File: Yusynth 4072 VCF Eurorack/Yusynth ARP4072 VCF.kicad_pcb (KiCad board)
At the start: 2 copper layers, 85 parts, among them J1 Audio In 1, J2 Audio In 2, J3 V/Oct, J4 CV 1, J5 CV 2, J6 Audio In 1, J7 CONN_02X05, Q1 MMDT3906, Q2 MMDT3906, Q3 MMDT3906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

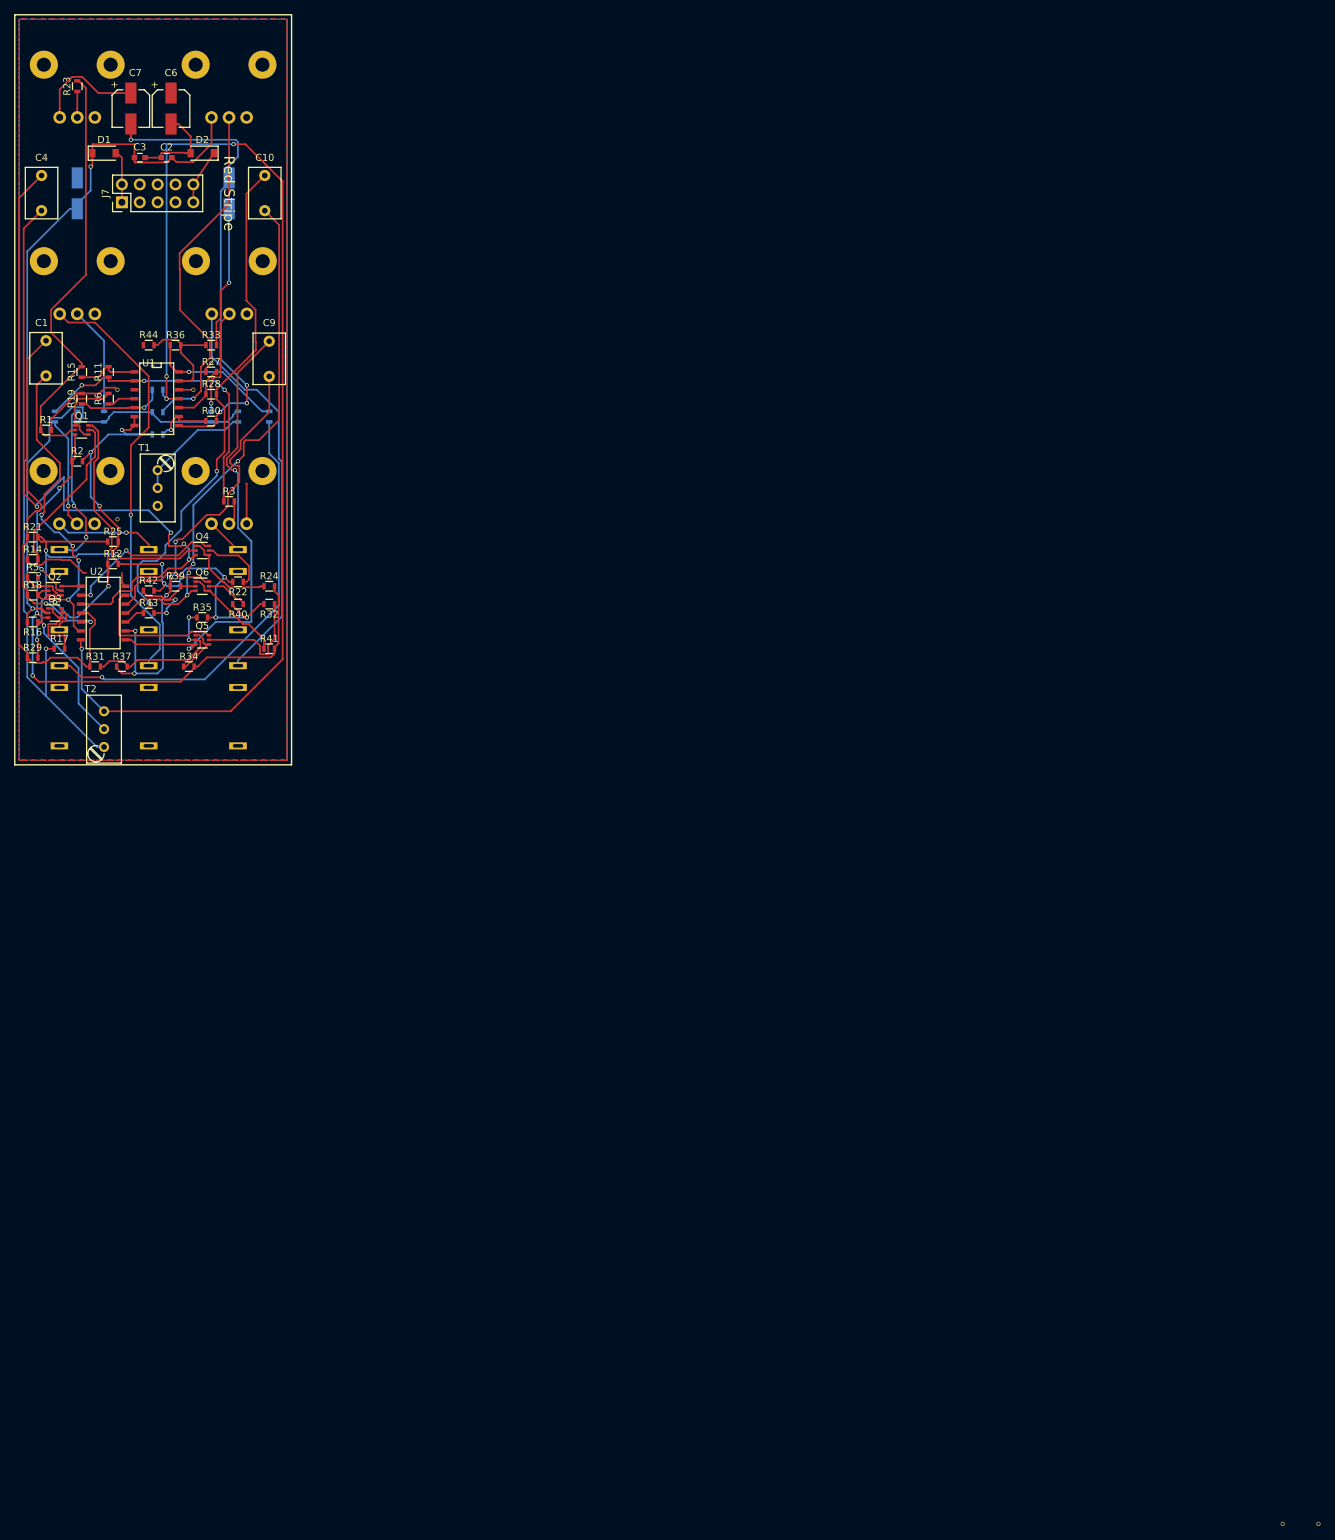
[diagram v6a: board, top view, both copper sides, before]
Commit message: Fixed some surprise DRC complaints
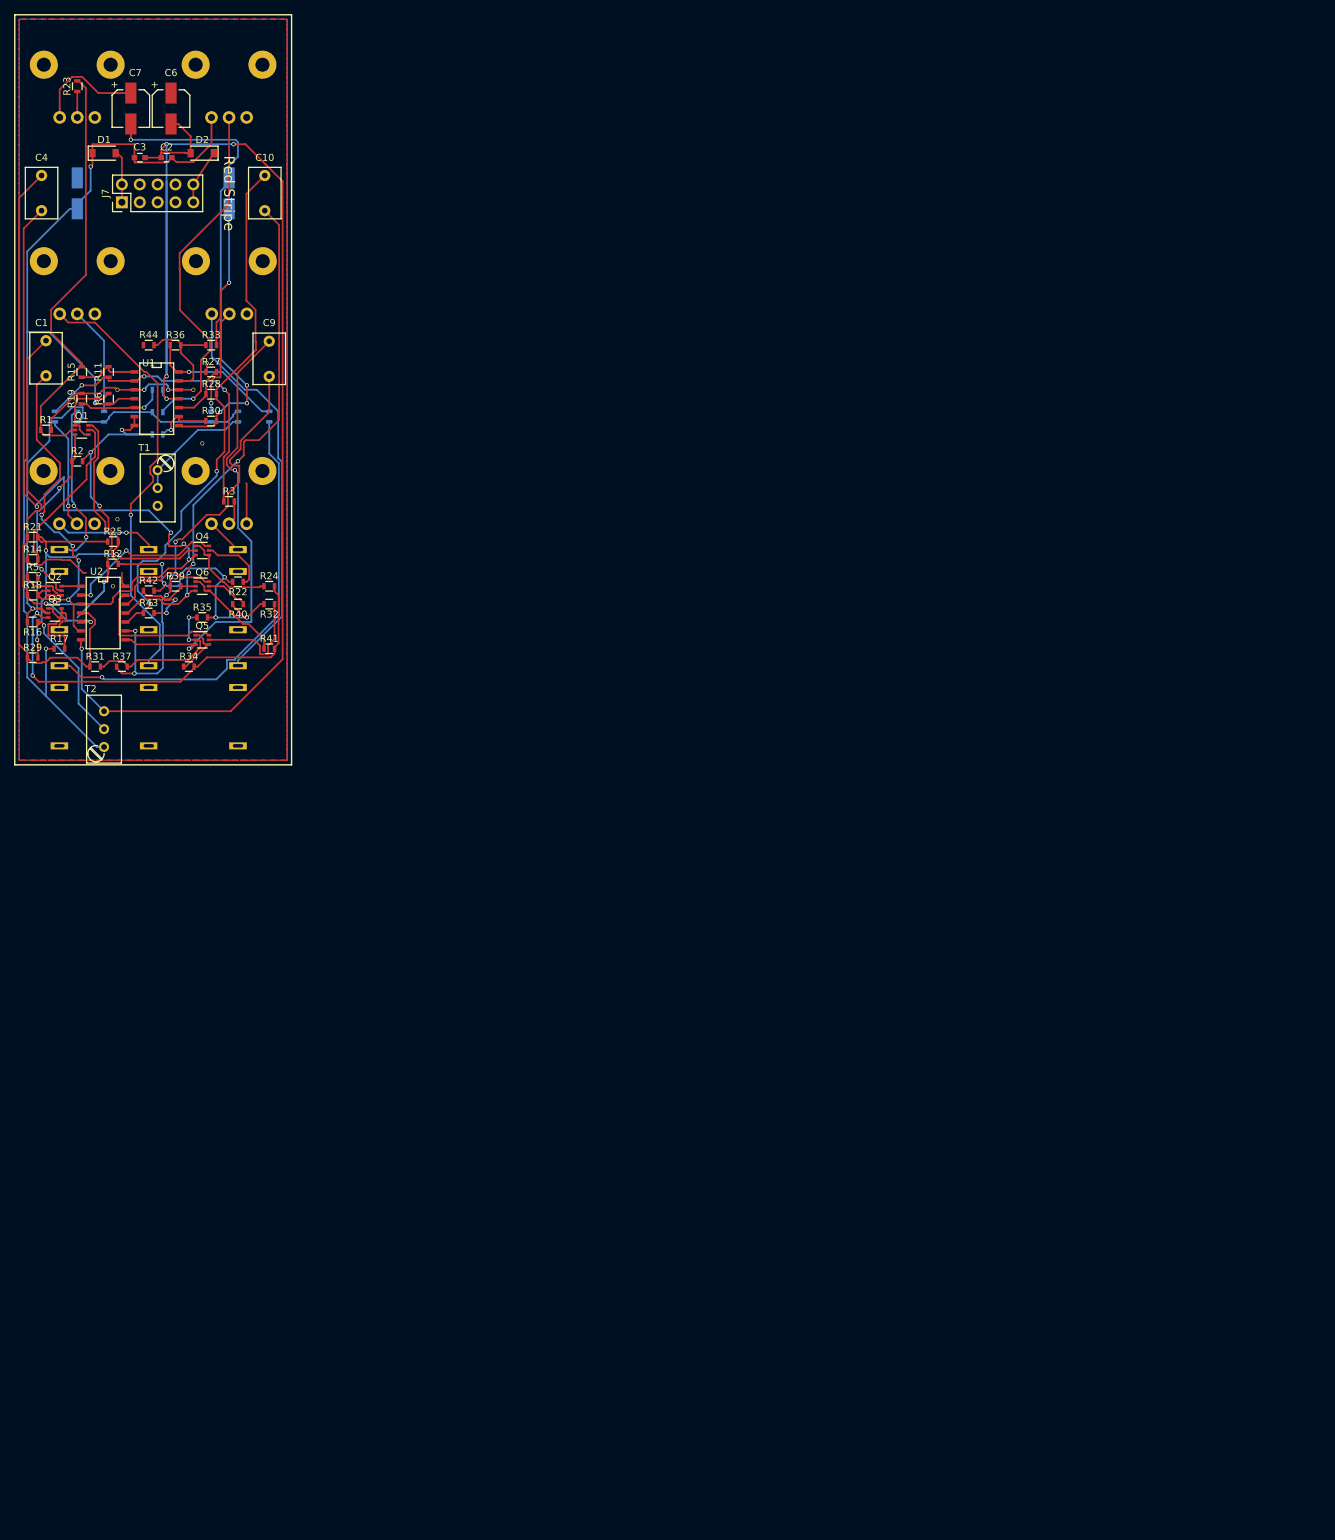
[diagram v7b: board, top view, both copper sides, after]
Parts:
- removed the REF** at (165.1, 135.3)
- removed the REF** at (170.2, 135.3)
- added REF**: VIA-0.6mm, YusynthLib:VIA-0.6mm, F.Cu at (181.6, 116.8)
- added REF**: VIA-0.6mm, YusynthLib:VIA-0.6mm, F.Cu at (168.9, 137.2)
- moved REF** 0.63 mm to (182.2, 105.4)
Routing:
- net -12V: track 180.2 -> 210.5 mm, vias 4 -> 5
- net +12V: track 132.5 -> 150.4 mm, vias 2 -> 3
- net Earth: track 39.0 -> 48.6 mm, vias 0 -> 2
- net Net-(Q1-Pad6): track 43.0 -> 45.3 mm
- net Net-(J6-Pad1): track 63.0 -> 64.6 mm
- net Net-(J5-Pad1): track 60.9 -> 62.5 mm
- net Net-(R11-Pad2): track 43.6 -> 44.2 mm

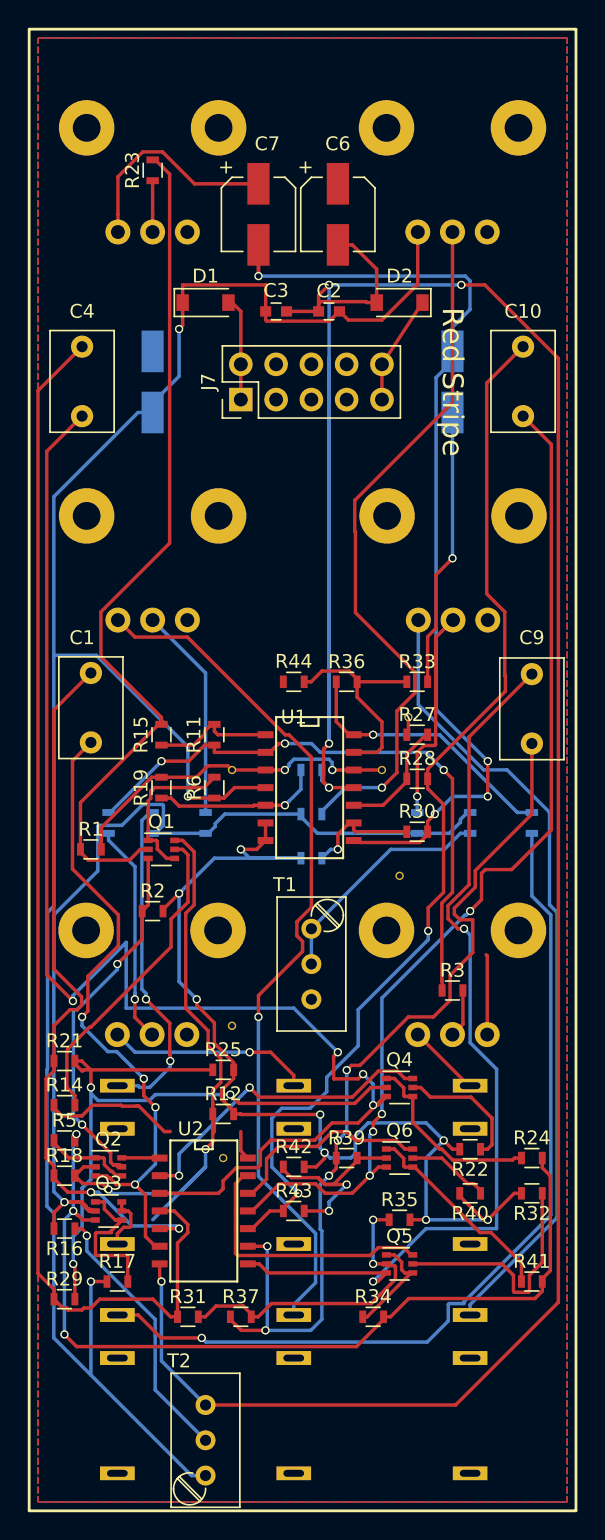
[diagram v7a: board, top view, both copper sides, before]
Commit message: Added holes in Thonkiconns, Resized for 100mm cuts, Rewired board
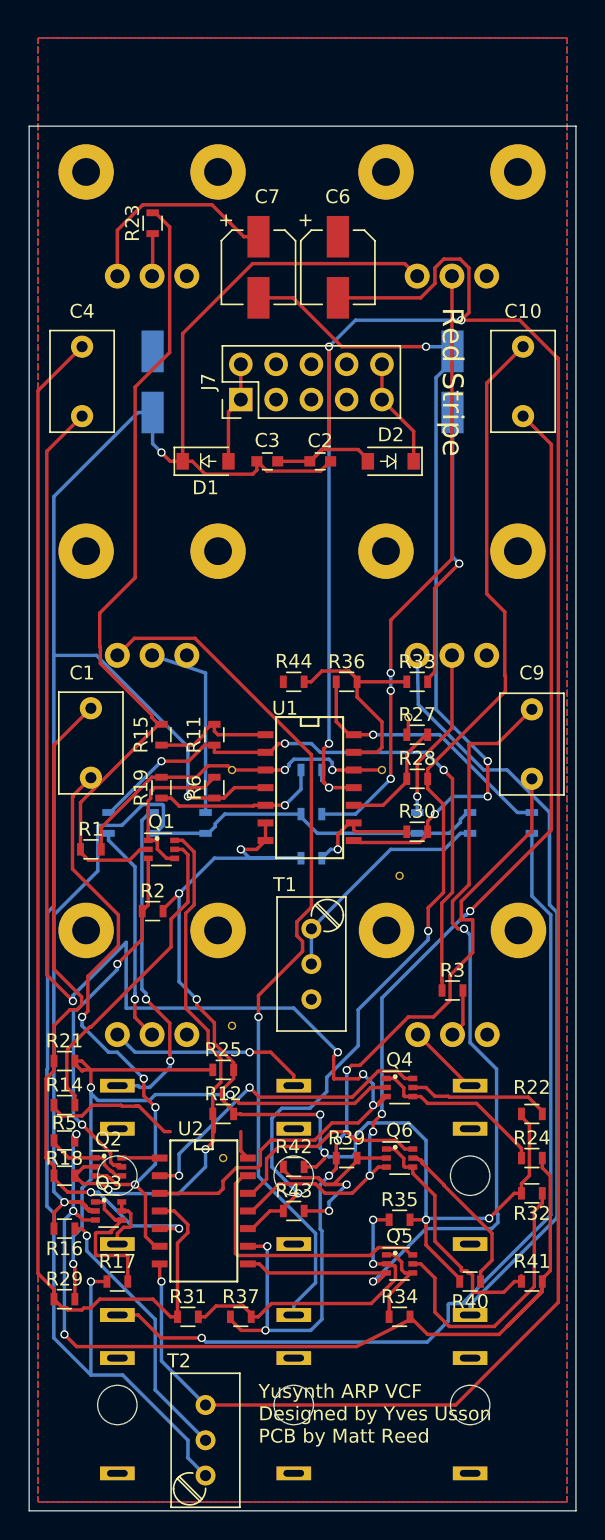
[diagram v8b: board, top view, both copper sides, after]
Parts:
- D1, D2: footprint Diodes_SMD:D_SOD-123 -> YusynthLib:D_SOD-123
- Q1, Q2, Q3, Q4, Q5, Q6: footprint TO_SOT_Packages_SMD:SOT-363_SC-70-6 -> YusynthLib:SOT-363_SC-70-6
- moved D2 11.4 mm to (181.0, 87.0)
- moved D1 11.4 mm to (167.6, 87.0)
- moved C2 10.8 mm to (175.9, 87.0)
- moved C3 10.8 mm to (172.1, 87.0)
- moved R40 6.35 mm to (186.7, 146.1)
- moved R22 5.12 mm to (191.1, 134.0)
- moved C6 3.81 mm to (177.2, 73.0)
- moved C7 3.81 mm to (171.4, 73.0)
- moved R23 3.81 mm to (163.8, 69.8)
- moved RV6 3.18 mm to (161.3, 73.7)
- moved RV3 3.18 mm to (182.9, 73.7)
- moved RV4 2.54 mm to (182.9, 101.0)
- moved RV5 2.54 mm to (161.3, 101.0)
- moved C1 2.54 mm to (159.4, 104.8)
- moved C9 2.54 mm to (191.1, 109.9)
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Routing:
- net -12V: track 210.5 -> 194.3 mm
- net +12V: track 150.4 -> 162.6 mm
- net Net-(C7-Pad2): track 71.7 -> 62.3 mm
- net Net-(R7-Pad2): track 50.9 -> 44.2 mm, vias 1 -> 3
- net Net-(Q6-Pad5): track 6.05 -> 12.1 mm
- net Earth: track 48.6 -> 42.8 mm
- net Net-(R12-Pad2): track 79.4 -> 85.0 mm, vias 8 -> 7
- net Net-(Q1-Pad6): track 45.3 -> 40.0 mm
- net Net-(Q3-Pad3): track 63.8 -> 68.8 mm
- net Net-(Q1-Pad2): track 62.3 -> 58.5 mm
- net Net-(Q6-Pad1): track 14.8 -> 18.1 mm
- net Net-(R9-Pad2): track 15.4 -> 12.4 mm
- net Net-(C9-Pad1): track 65.8 -> 63.0 mm
- net Net-(Q5-Pad5): track 17.4 -> 20.2 mm
- net Net-(C1-Pad1): track 51.9 -> 49.4 mm
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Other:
- board outline added: 39.4 x 99.7 mm
- board text added: "Yusynth ARP VCF Designed by Yves Usson PCB by Matt Reed"
